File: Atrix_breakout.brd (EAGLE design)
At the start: 8.2 x 17 mm, 8 parts

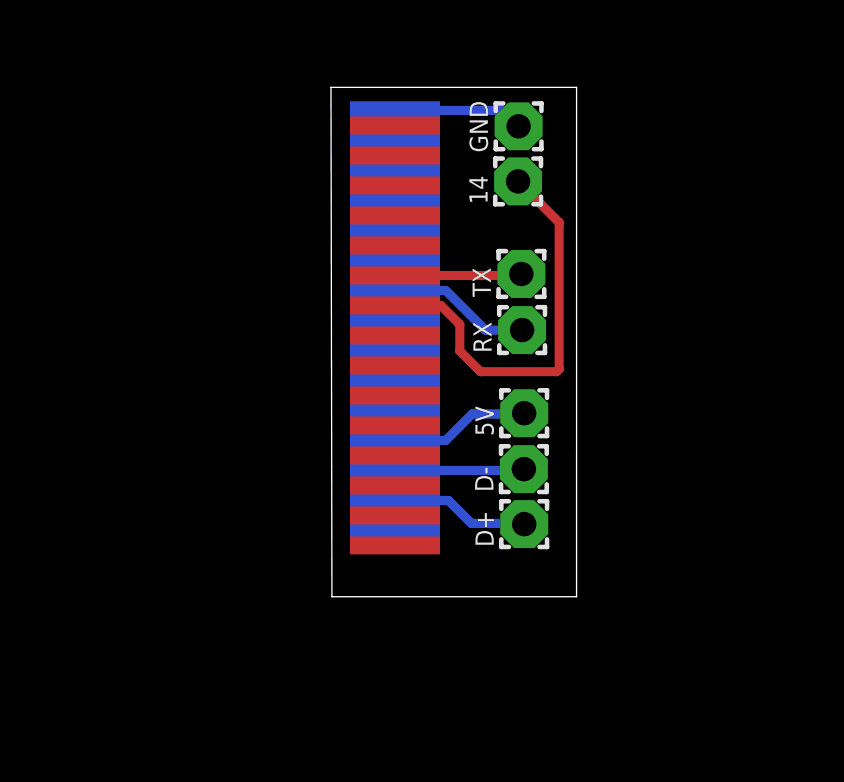
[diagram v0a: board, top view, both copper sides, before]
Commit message: Update README with How-to
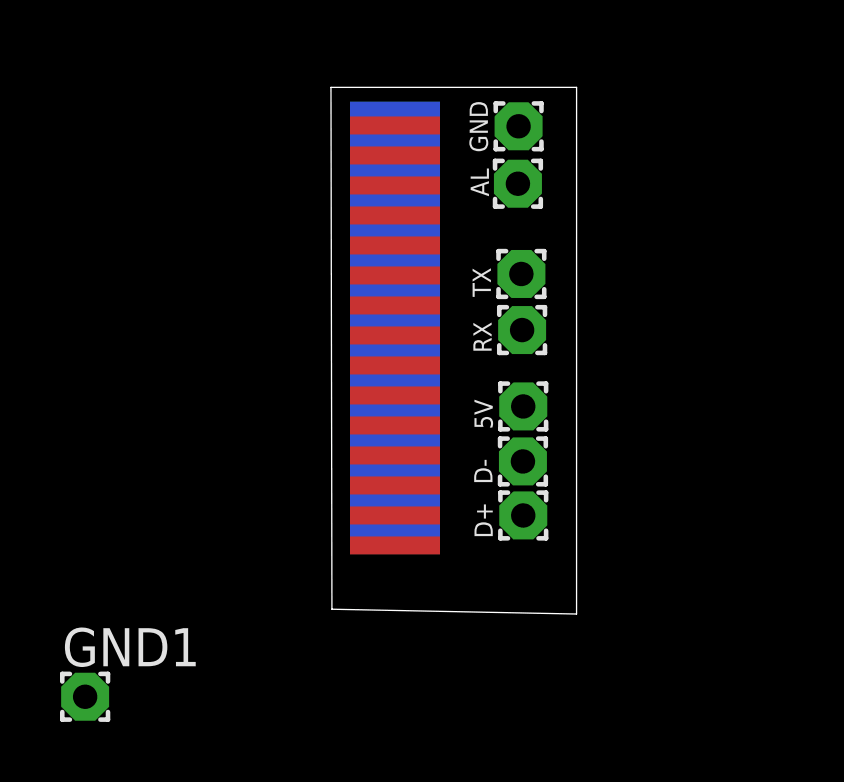
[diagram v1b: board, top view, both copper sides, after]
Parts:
- removed 14: (no value), wirepad:1,6/0,8
- added AL, GND1: (no value), wirepad:1,6/0,8
- moved D+ 0.29 mm to (4.38, 6.73)
- moved D- 0.26 mm to (4.37, 8.53)
- moved 5V 0.23 mm to (4.38, 10.4)
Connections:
- removed net N$5: 14.1, U$1.14
- new net N$2: AL.1, U$1.21
- net N$1: now also GND1.1
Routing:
- net N$5: track 13.8 -> 0.00 mm
- net N$6: track 4.79 -> 0.00 mm
- net N$8: track 4.68 -> 0.00 mm
- net N$4: track 4.63 -> 0.00 mm
- net N$1: track 4.34 -> 0.00 mm
- net N$3: track 4.32 -> 0.00 mm
- net N$7: track 4.23 -> 0.00 mm
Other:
- board size 8.2 x 17 mm -> 8.2 x 17.6 mm
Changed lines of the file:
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@@
 <board>
 <plain>
-<wire x1="-1.999653125" y1="4.02215625" x2="6.154371875" y2="4.022153125" width="0" layer="20"/>
-<wire x1="6.154371875" y1="4.022153125" x2="6.15530625" y2="21.001078125" width="0" layer="20"/>
+<wire x1="-1.999653125" y1="3.6061375" x2="6.154371875" y2="3.446128125" width="0" layer="20"/>
+<wire x1="6.154371875" y1="3.446128125" x2="6.15530625" y2="21.001078125" width="0" layer="20"/>
 <wire x1="6.15530625" y1="21.001078125" x2="-2.031359375" y2="21.001075" width="0" layer="20"/>
-<wire x1="-2.031359375" y1="21.001075" x2="-1.999653125" y2="4.02215625" width="0" layer="20"/>
+<wire x1="-2.031359375" y1="21.001075" x2="-1.999653125" y2="3.6061375" width="0" layer="20"/>
 </plain>
 <attributes>
@@
 <attribute name="VALUE" x="3.62245625" y="19.703559375" size="0.0254" layer="27" rot="R90"/>
 </element>
-<element name="D-" library="wirepad" package="1,6/0,8" value="" x="4.399028125" y="8.27608125" smashed="yes" rot="R90">
-<attribute name="NAME" x="3.383028125" y="7.51408125" size="0.6096" layer="25" ratio="10" rot="R90"/>
-<attribute name="VALUE" x="3.799028125" y="8.27608125" size="0.0254" layer="27" rot="R90"/>
-</element>
-<element name="D+" library="wirepad" package="1,6/0,8" value="" x="4.40951875" y="6.44294375" smashed="yes" rot="R90">
-<attribute name="NAME" x="3.39351875" y="5.68094375" size="0.6096" layer="25" ratio="10" rot="R90"/>
-<attribute name="VALUE" x="3.80951875" y="6.44294375" size="0.0254" layer="27" rot="R90"/>
-</element>
-<element name="14" library="wirepad" package="1,6/0,8" value="" x="4.20589375" y="17.86703125" smashed="yes" rot="R90">
-<attribute name="NAME" x="3.18989375" y="17.10503125" size="0.6096" layer="25" ratio="10" rot="R90"/>
-<attribute name="VALUE" x="3.60589375" y="17.86703125" size="0.0254" layer="27" rot="R90"/>
+<element name="D-" library="wirepad" package="1,6/0,8" value="" x="4.3670625" y="8.532090625" smashed="yes" rot="R90">
+<attribute name="NAME" x="3.3510625" y="7.770090625" size="0.6096" layer="25" ratio="10" rot="R90"/>
+<attribute name="VALUE" x="3.7670625" y="8.532090625" size="0.0254" layer="27" rot="R90"/>
+</element>
+<element name="D+" library="wirepad" package="1,6/0,8" value="" x="4.37755625" y="6.73095625" smashed="yes" rot="R90">
+<attribute name="NAME" x="3.36155625" y="5.96895625" size="0.6096" layer="25" ratio="10" rot="R90"/>
+<attribute name="VALUE" x="3.77755625" y="6.73095625" size="0.0254" layer="27" rot="R90"/>
 </element>
 <element name="RX" library="wirepad" package="1,6/0,8" value="" x="4.339765625" y="12.911321875" smashed="yes" rot="R90">
@@
 <attribute name="VALUE" x="3.714975" y="14.7807" size="0.0254" layer="27" rot="R90"/>
 </element>
-<element name="5V" library="wirepad" package="1,6/0,8" value="" x="4.408721875" y="10.14095625" smashed="yes" rot="R90">
-<attribute name="NAME" x="3.392721875" y="9.37895625" size="0.6096" layer="25" ratio="10" rot="R90"/>
-<attribute name="VALUE" x="3.808721875" y="10.14095625" size="0.0254" layer="27" rot="R90"/>
-</element>
+<element name="5V" library="wirepad" package="1,6/0,8" value="" x="4.376759375" y="10.364965625" smashed="yes" rot="R90">
+<attribute name="NAME" x="3.360759375" y="9.602965625" size="0.6096" layer="25" ratio="10" rot="R90"/>
+<attribute name="VALUE" x="3.776759375" y="10.364965625" size="0.0254" layer="27" rot="R90"/>
+</element>
+<element name="AL" library="wirepad" package="1,6/0,8" value="" x="4.1998375" y="17.78889375" smashed="yes" rot="R90">
+<attribute name="NAME" x="3.2342375" y="17.367115625" size="0.6096" layer="25" ratio="10" rot="R90"/>
+<attribute name="VALUE" x="3.5998375" y="17.78889375" size="0.0254" layer="27" rot="R90"/>
+</element>
+<element name="GND1" library="wirepad" package="1,6/0,8" value="" x="-10.226028125" y="0.68844375"/>
 </elements>
 <signals>
@@
 <contactref element="U$1" pad="1"/>
 <contactref element="GND" pad="1"/>
-<wire x1="0.102371875" y1="20.231275" x2="3.694740625" y2="20.231275" width="0.3048" layer="16"/>
-<wire x1="3.694740625" y1="20.231275" x2="4.22245625" y2="19.703559375" width="0.3048" layer="16"/>
+<contactref element="GND1" pad="1"/>
+<wire x1="0.102371875" y1="20.231275" x2="4.22245625" y2="19.703559375" width="0" layer="19" extent="16-16"/>
+<wire x1="-10.226028125" y1="0.68844375" x2="0.102371875" y2="20.231275" width="0" layer="19" extent="16-16"/>
 </signal>
 <signal name="N$3">
 <contactref element="U$1" pad="25"/>
 <contactref element="D-" pad="1"/>
-<wire x1="0.102371875" y1="8.231275" x2="4.354221875" y2="8.231275" width="0.3048" layer="16"/>
-<wire x1="4.354221875" y1="8.231275" x2="4.399028125" y2="8.27608125" width="0.3048" layer="16"/>
+<wire x1="0.102371875" y1="8.231275" x2="4.3670625" y2="8.532090625" width="0" layer="19" extent="16-16"/>
 </signal>
 <signal name="N$4">
 <contactref element="U$1" pad="27"/>
 <contactref element="D+" pad="1"/>
-<wire x1="0.102371875" y1="7.231275" x2="1.885421875" y2="7.231275" width="0.3048" layer="16"/>
-<wire x1="1.885421875" y1="7.231275" x2="2.64985625" y2="6.466840625" width="0.3048" layer="16"/>
-<wire x1="2.64985625" y1="6.466840625" x2="4.385621875" y2="6.466840625" width="0.3048" layer="16"/>
-<wire x1="4.385621875" y1="6.466840625" x2="4.40951875" y2="6.44294375" width="0.3048" layer="16"/>
-</signal>
-<signal name="N$5">
-<contactref element="U$1" pad="14"/>
-<contactref element="14" pad="1"/>
-<wire x1="0.102371875" y1="13.731275" x2="1.631640625" y2="13.731275" width="0.3048" layer="1"/>
-<wire x1="1.631640625" y1="13.731275" x2="2.26341875" y2="13.099496875" width="0.3048" layer="1"/>
-<wire x1="2.26341875" y1="13.099496875" x2="2.26341875" y2="12.21430625" width="0.3048" layer="1"/>
-<wire x1="2.26341875" y1="12.21430625" x2="2.953484375" y2="11.524240625" width="0.3048" layer="1"/>
-<wire x1="2.953484375" y1="11.524240625" x2="5.492828125" y2="11.524240625" width="0.3048" layer="1"/>
-<wire x1="5.492828125" y1="11.524240625" x2="5.5757375" y2="11.60715" width="0.3048" layer="1"/>
-<wire x1="5.5757375" y1="11.60715" x2="5.5757375" y2="16.4971875" width="0.3048" layer="1"/>
-<wire x1="5.5757375" y1="16.4971875" x2="4.20589375" y2="17.86703125" width="0.3048" layer="1"/>
+<wire x1="0.102371875" y1="7.231275" x2="4.37755625" y2="6.73095625" width="0" layer="19" extent="16-16"/>
 </signal>
 <signal name="N$6">
 <contactref element="U$1" pad="13"/>
 <contactref element="RX" pad="1"/>
-<wire x1="0.102371875" y1="14.231275" x2="1.79386875" y2="14.231275" width="0.3048" layer="16"/>
-<wire x1="1.79386875" y1="14.231275" x2="3.1191" y2="12.90604375" width="0.3048" layer="16"/>
-<wire x1="3.1191" y1="12.90604375" x2="4.3344875" y2="12.90604375" width="0.3048" layer="16"/>
-<wire x1="4.3344875" y1="12.90604375" x2="4.339765625" y2="12.911321875" width="0.3048" layer="16"/>
+<wire x1="0.102371875" y1="14.231275" x2="4.339765625" y2="12.911321875" width="0" layer="19" extent="16-16"/>
 </signal>
 <signal name="N$7">
 <contactref element="U$1" pad="12"/>
 <contactref element="TX" pad="1"/>
-<wire x1="0.102371875" y1="14.731275" x2="4.26555" y2="14.731275" width="0.3048" layer="1"/>
-<wire x1="4.26555" y1="14.731275" x2="4.314975" y2="14.7807" width="0.3048" layer="1"/>
+<wire x1="0.102371875" y1="14.731275" x2="4.314975" y2="14.7807" width="0" layer="19" extent="1-1"/>
 </signal>
 <signal name="N$8">
 <contactref element="U$1" pad="23"/>
 <contactref element="5V" pad="1"/>
-<wire x1="0.102371875" y1="9.231275" x2="1.793928125" y2="9.231275" width="0.3048" layer="16"/>
-<wire x1="1.793928125" y1="9.231275" x2="2.67745625" y2="10.114803125" width="0.3048" layer="16"/>
-<wire x1="2.67745625" y1="10.114803125" x2="4.38256875" y2="10.114803125" width="0.3048" layer="16"/>
-<wire x1="4.38256875" y1="10.114803125" x2="4.408721875" y2="10.14095625" width="0.3048" layer="16"/>
+<wire x1="0.102371875" y1="9.231275" x2="4.376759375" y2="10.364965625" width="0" layer="19" extent="16-16"/>
+</signal>
+<signal name="N$2">
+<contactref element="U$1" pad="21"/>
+<contactref element="AL" pad="1"/>
+<wire x1="0.102371875" y1="10.231275" x2="4.1998375" y2="17.78889375" width="0" layer="19" extent="16-16"/>
 </signal>
 </signals>

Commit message: updates
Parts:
- moved GND1 17.5 mm to (4.28, 10.4), turned to 90 degrees
- moved D+ 1.81 mm to (4.28, 4.92)
- moved 5V 1.74 mm to (4.26, 8.63)
- moved D- 1.72 mm to (4.26, 6.81)
- moved RX 0.65 mm to (4.19, 13.5)
- moved TX 0.63 mm to (4.18, 15.4)
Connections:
- net N$1 renamed GND
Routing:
- net GND: track 0.00 -> 16.4 mm
- net N$2: track 0.00 -> 12.0 mm
- net N$4: track 0.00 -> 5.62 mm
- net N$3: track 0.00 -> 4.74 mm
- net N$8: track 0.00 -> 4.41 mm
- net N$6: track 0.00 -> 4.37 mm
- net N$7: track 0.00 -> 4.36 mm
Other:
- board size 8.2 x 17.6 mm -> 8.1 x 17.4 mm

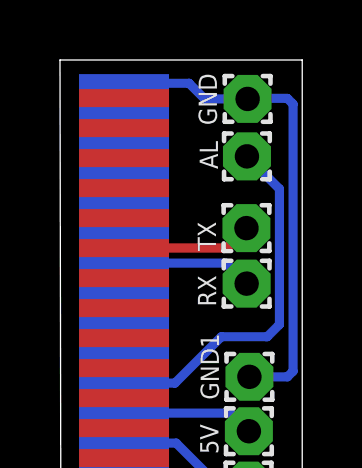
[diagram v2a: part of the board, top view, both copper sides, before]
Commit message: Correct AL pin name, should be ACC
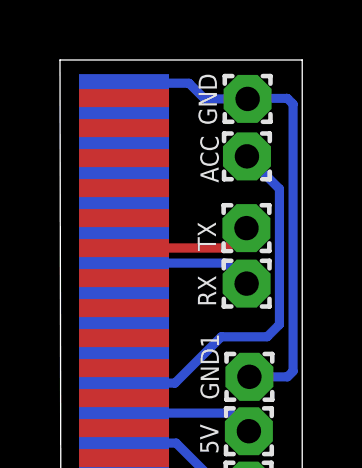
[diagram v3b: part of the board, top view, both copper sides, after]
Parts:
- renumbered AL to ACC
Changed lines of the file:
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@@
 <attribute name="VALUE" x="3.66481875" y="8.627259375" size="0.0254" layer="27" rot="R90"/>
 </element>
-<element name="AL" library="wirepad" package="1,6/0,8" value="" x="4.1998375" y="17.78889375" smashed="yes" rot="R90">
-<attribute name="NAME" x="3.2342375" y="17.367115625" size="0.6096" layer="25" ratio="10" rot="R90"/>
+<element name="ACC" library="wirepad" package="1,6/0,8" value="" x="4.1998375" y="17.78889375" smashed="yes" rot="R90">
+<attribute name="NAME" x="3.258146875" y="16.91235" size="0.6096" layer="25" ratio="10" rot="R90"/>
 <attribute name="VALUE" x="3.5998375" y="17.78889375" size="0.0254" layer="27" rot="R90"/>
 </element>
@@
 <signal name="N$2">
 <contactref element="U$1" pad="21"/>
-<contactref element="AL" pad="1"/>
+<contactref element="ACC" pad="1"/>
 <wire x1="0.102371875" y1="10.231275" x2="1.80234375" y2="10.231275" width="0.3048" layer="16"/>
 <wire x1="1.80234375" y1="10.231275" x2="3.347084375" y2="11.776015625" width="0.3048" layer="16"/>

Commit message: Push to OpenJB
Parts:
- removed 5V, D+, D-, GND1, RX, TX: (no value), wirepad:1,6/0,8
- added JP1: FTDI, SparkFun-Connectors:FTDI_BASIC
- added U$2: (no value), SparkFun-Aesthetics:OSHW-LOGO-S
- added X1: USB-MICROB, Pinoccio:USB-MICROB
- ACC, GND: device wirepad:1,6/0,8 -> wirepad:1,6/0,9
- moved GND 7.12 mm to (10.7, 16.8), turned to 180 degrees
- moved ACC 4.52 mm to (8.61, 16.8), turned to 180 degrees
- moved U$1 0.21 mm to (0.18, 12.5)
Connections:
- removed net N$3: D-.1, U$1.25
- removed net N$4: D+.1, U$1.27
- removed net N$6: RX.1, U$1.13
- removed net N$7: TX.1, U$1.12
- removed net N$8: 5V.1, U$1.23
- new net 5V: U$1.23, X1.VBUS
- new net D+: U$1.27, X1.D+
- new net D-: U$1.25, X1.D-
- new net RX: JP1.TXO, U$1.13
- new net TX: JP1.RXI, U$1.12
- net GND: now also JP1.GND, X1.GND; no longer GND1.1
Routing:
- net GND: track 16.4 -> 32.6 mm, vias 0 -> 1
- net D+: track 0.00 -> 9.87 mm
- net D-: track 0.00 -> 9.64 mm, vias 0 -> 2
- net 5V: track 0.00 -> 9.28 mm
- net TX: track 0.00 -> 5.75 mm
- net N$4: track 5.62 -> 0.00 mm
- net RX: track 0.00 -> 5.13 mm
- net N$3: track 4.74 -> 0.00 mm
- net N$8: track 4.41 -> 0.00 mm
- net N$6: track 4.37 -> 0.00 mm
- net N$7: track 4.36 -> 0.00 mm
- net N$1: track 12.0 -> 13.0 mm
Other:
- board size 8.1 x 17.4 mm -> 14.7 x 17.4 mm
- board text added: "Atrix - v0.2 https://github.com/haifisch/atrix"
